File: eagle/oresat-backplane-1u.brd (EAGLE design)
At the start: 82.5 x 213.5 mm, 35 parts

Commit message: oresat-backplane-1u.sch
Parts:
- moved C3 114.5 mm to (32.3, 14.3)
- moved C4 114.5 mm to (42.5, 14.3)
- moved CF2.1 114.5 mm to (13.2, 82.1)
- moved CF2.2 114.5 mm to (41.2, 82.1)
- moved CF2.3 114.5 mm to (19.6, 92.1)
- moved CF3.1 114.5 mm to (13.2, 72.1)
- moved CF3.2 114.5 mm to (41.2, 72.1)
- moved CF4.1 114.5 mm to (13.2, 62.1)
- moved CF4.2 114.5 mm to (41.2, 62.1)
- moved CF5.1 114.5 mm to (13.2, 52.1)
- moved CF5.2 114.5 mm to (41.2, 52.1)
- moved CF6.1 114.5 mm to (13.2, 42.1)
- moved CF6.2 114.5 mm to (41.2, 42.1)
- moved CF7.1 114.5 mm to (13.2, 32.1)
- moved CF7.2 114.5 mm to (41.2, 32.1)
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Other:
- board size 82.5 x 213.5 mm -> 82.5 x 99 mm
- board text added: "OreSat 1U Backplane v1.0 (Frame 1.1)"
- board text removed: "OreSat Backplane v2.1 (Frame 1.1)"

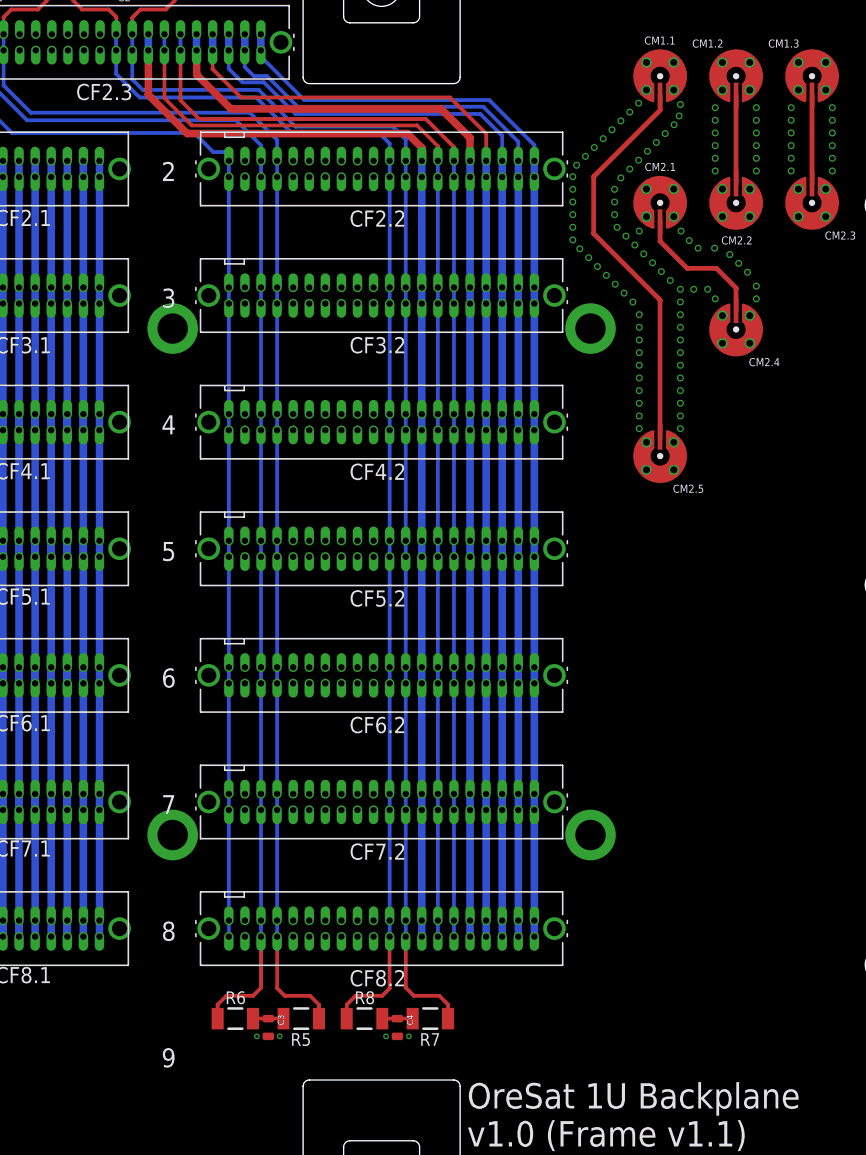
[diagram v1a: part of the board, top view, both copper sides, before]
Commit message: TNAMES cleanup, renamed by card number.
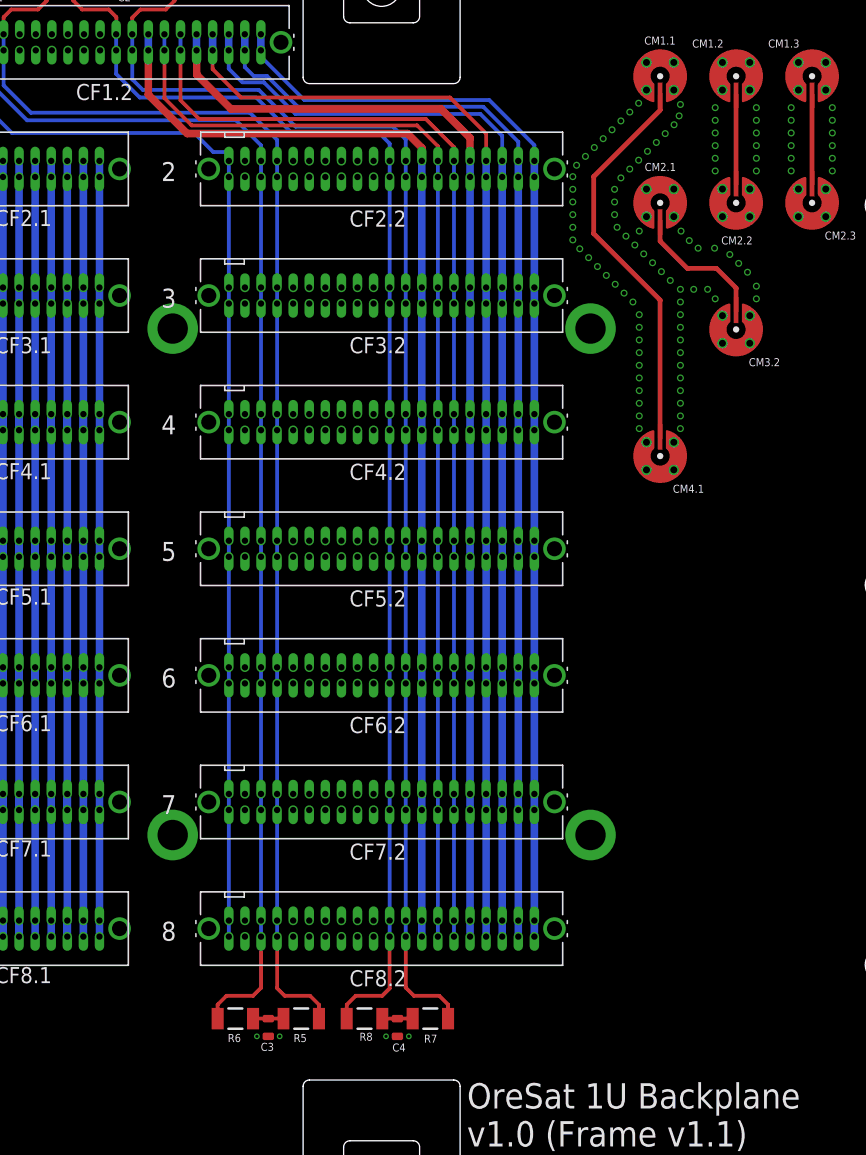
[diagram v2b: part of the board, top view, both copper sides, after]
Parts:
- renumbered CF2.3 to CF1.2, CM2.4 to CM3.2, CM2.5 to CM4.1

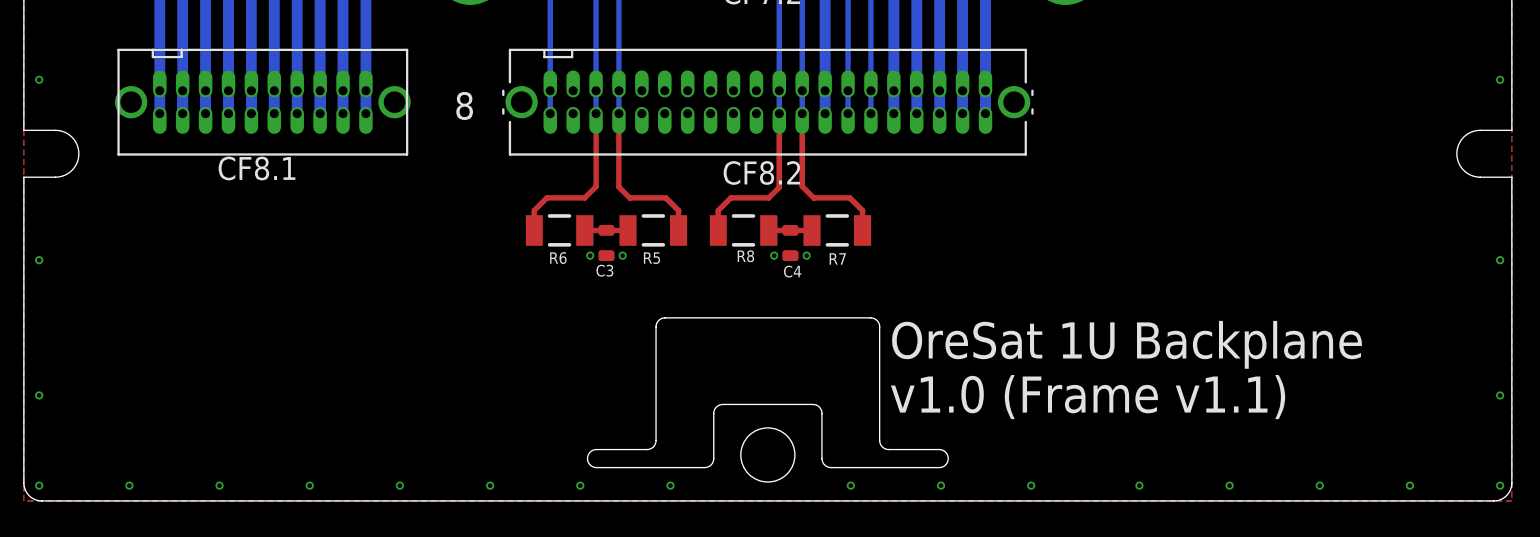
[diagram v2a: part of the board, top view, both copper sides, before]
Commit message: Added 1U -Z end cap connector.
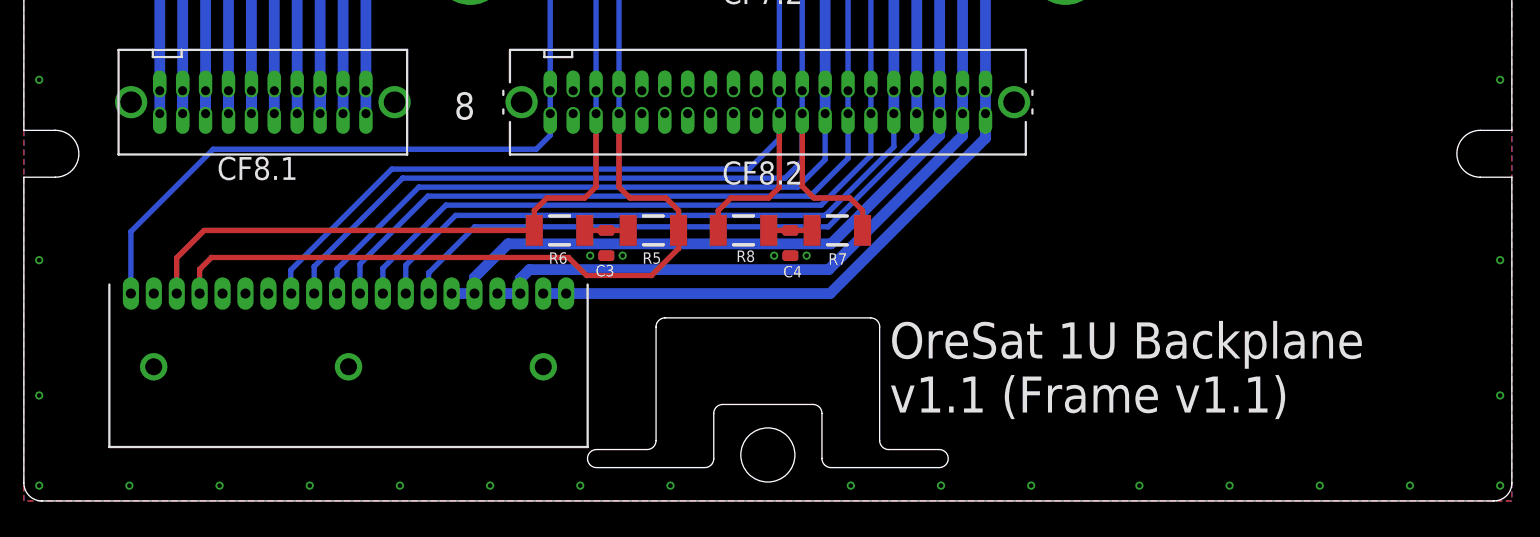
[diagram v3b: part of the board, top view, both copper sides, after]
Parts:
- added J1: 5-104196-5, J-TE-5-104196-5-RA-1.27mm-female-th:5-104196-5
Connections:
- removed net SPARE1: CF1.2.10, CF1.2.9, CF2.2.10, CF2.2.9, CF3.2.10, CF3.2.9, CF4.2.10, CF4.2.9, CF5.2.10, CF5.2.9, CF6.2.10, CF6.2.9, CF7.2.10, CF7.2.9, CF8.2.10, CF8.2.9
- removed net SPARE3: CF1.2.5, CF1.2.6, CF2.2.5, CF2.2.6, CF3.2.5, CF3.2.6, CF4.2.5, CF4.2.6, CF5.2.5, CF5.2.6, CF6.2.5, CF6.2.6, CF7.2.5, CF7.2.6, CF8.2.5, CF8.2.6
- removed net SPARE4: CF1.2.3, CF1.2.4, CF2.2.3, CF2.2.4, CF3.2.3, CF3.2.4, CF4.2.3, CF4.2.4, CF5.2.3, CF5.2.4, CF6.2.3, CF6.2.4, CF7.2.3, CF7.2.4, CF8.2.3, CF8.2.4
- removed net SPARE5: CF1.2.1, CF1.2.2, CF2.2.1, CF2.2.2, CF3.2.1, CF3.2.2, CF4.2.1, CF4.2.2, CF5.2.1, CF5.2.2, CF6.2.1, CF6.2.2, CF7.2.1, CF7.2.2, CF8.2.1, CF8.2.2
- new net SPARE1-TURNSTILE-DPLY: CF1.2.10, CF1.2.9, CF2.2.10, CF2.2.9, CF3.2.10, CF3.2.9, CF4.2.10, CF4.2.9, CF5.2.10, CF5.2.9, CF6.2.10, CF6.2.9, CF7.2.10, CF7.2.9, CF8.2.10, CF8.2.9, J1.13
- new net SPARE3-MAG-PWR: CF1.2.5, CF1.2.6, CF2.2.5, CF2.2.6, CF3.2.5, CF3.2.6, CF4.2.5, CF4.2.6, CF5.2.5, CF5.2.6, CF6.2.5, CF6.2.6, CF7.2.5, CF7.2.6, CF8.2.5, CF8.2.6, J1.15, J1.16
- new net SPARE4-MAG-SCL: CF1.2.3, CF1.2.4, CF2.2.3, CF2.2.4, CF3.2.3, CF3.2.4, CF4.2.3, CF4.2.4, CF5.2.3, CF5.2.4, CF6.2.3, CF6.2.4, CF7.2.3, CF7.2.4, CF8.2.3, CF8.2.4, J1.17, J1.18
- new net SPARE5-MAG-SDA: CF1.2.1, CF1.2.2, CF2.2.1, CF2.2.2, CF3.2.1, CF3.2.2, CF4.2.1, CF4.2.2, CF5.2.1, CF5.2.2, CF6.2.1, CF6.2.2, CF7.2.1, CF7.2.2, CF8.2.1, CF8.2.2, J1.19, J1.20
- net !SD: now also J1.1
- net CAN1_H: now also J1.4
- net CAN1_L: now also J1.3
- net CAN2_H: now also J1.9
- net CAN2_L: now also J1.8
- net GND: now also J1.2, J1.5, J1.6, J1.HD1, J1.HD2, J1.HD3
- net OPD_PWR: now also J1.10
- net OPD_SCL: now also J1.11
- net OPD_SDA: now also J1.12
- net SPARE2: now also J1.14
- net VBUS: now also J1.7
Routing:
- net SPARE1-TURNSTILE-DPLY: track 0.00 -> 123.1 mm
- net SPARE3-MAG-PWR: track 0.00 -> 122.2 mm
- net SPARE4-MAG-SCL: track 0.00 -> 120.5 mm
- net SPARE5-MAG-SDA: track 0.00 -> 118.2 mm
- net SPARE1: track 89.9 -> 0.00 mm
- net SPARE3: track 89.8 -> 0.00 mm
- net SPARE4: track 89.4 -> 0.00 mm
- net SPARE5: track 88.8 -> 0.00 mm
- net OPD_SCL: track 90.6 -> 124.2 mm
- net CAN2_H: track 105.4 -> 139.0 mm
- net OPD_PWR: track 90.4 -> 123.9 mm
- net OPD_SDA: track 90.7 -> 124.1 mm
- net CAN2_L: track 105.2 -> 138.0 mm
- net SPARE2: track 89.9 -> 122.5 mm
- net VBUS: track 0.00 -> 31.8 mm
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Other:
- board text added: "OreSat 1U Backplane v1.1 (Frame v1.1)"
- board text removed: "OreSat 1U Backplane v1.0 (Frame v1.1)"

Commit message: Backplane v1.1!
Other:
- board text added: "OreSat 1U Backplane v1.1 (Frame 1.1)"
- board text removed: "OreSat 1U Backplane v1.0 (Frame 1.1)"
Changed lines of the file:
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@@
 v1.1 (Frame v1.1)</text>
 <text x="34.35" y="4.85" size="2" layer="22" font="vector" rot="MR0">OreSat 1U Backplane
-v1.0 (Frame 1.1)</text>
+v1.1 (Frame 1.1)</text>
 <wire x1="75.75" y1="95.25" x2="6.75" y2="95.25" width="0.001" layer="52"/>
 <wire x1="6.75" y1="95.25" x2="4.25" y2="92.75" width="0.001" layer="52" curve="90"/>

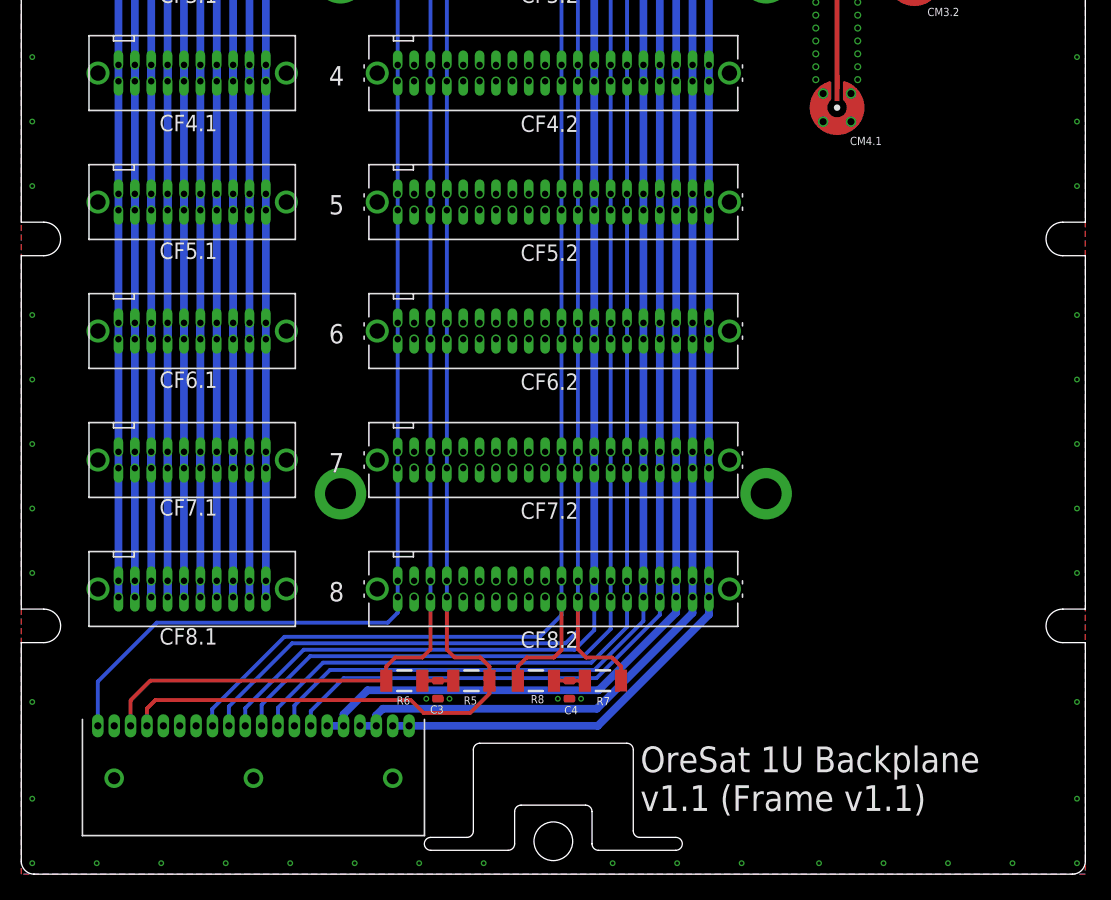
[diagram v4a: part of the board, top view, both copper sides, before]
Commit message: Updated 1U backplane to v1.2. Better position of end cap connector, added debug connector.
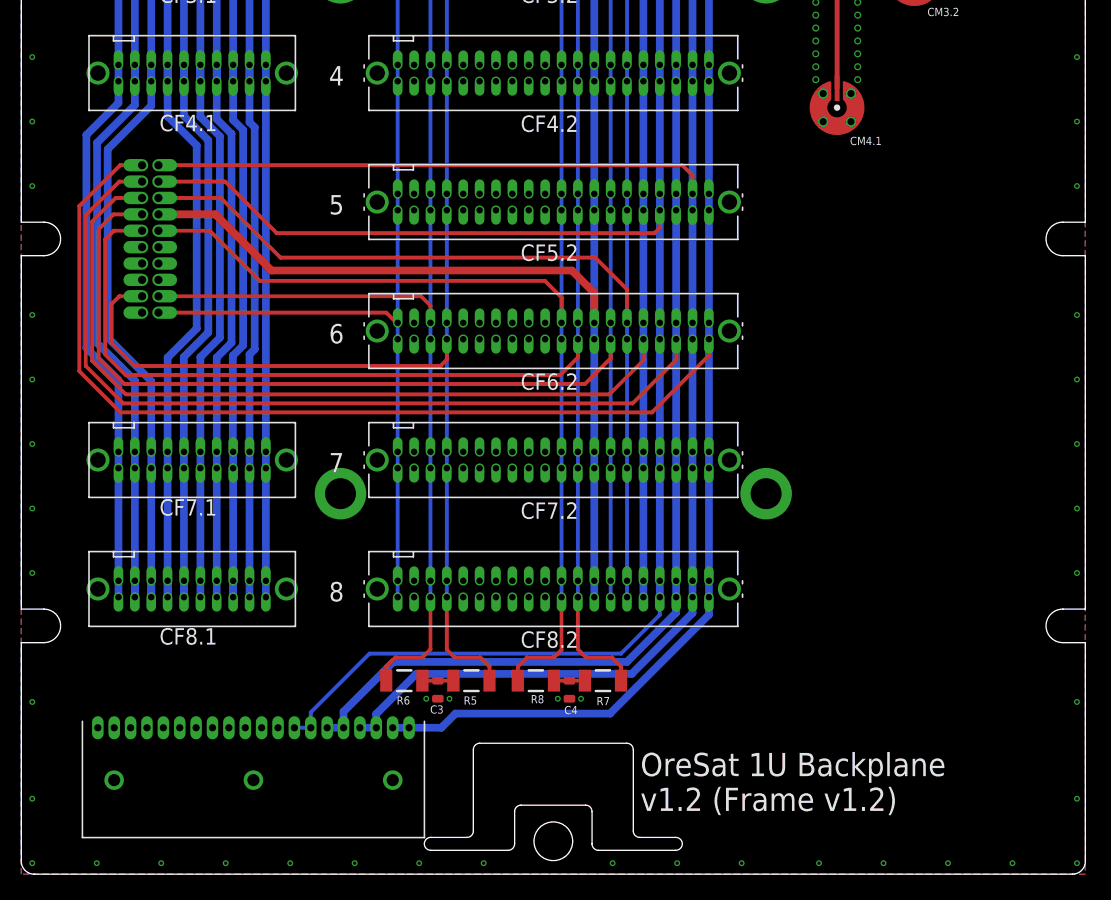
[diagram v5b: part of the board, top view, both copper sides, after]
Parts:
- removed CF5.1, CF6.1: SFM-110-X1-XXX-D-LC, J-Samtec-SFM-110-X1-XXX-D-LC:SFM-110-X1-XXX-D-LC
- added J3: HARWIN-M50-3002045, J-Harwin-M50-3002045-20pin-1.27-F-vertical:HARWIN-M50-30020452
- moved J1 0.15 mm to (18.0, 11.3)
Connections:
- net !SD: now also J3.20; no longer J1.1
- net AUX-1: no longer CF5.1.1, CF5.1.2, CF6.1.1, CF6.1.2
- net AUX-10: no longer CF5.1.19, CF5.1.20, CF6.1.19, CF6.1.20
- net AUX-2: no longer CF5.1.3, CF5.1.4, CF6.1.3, CF6.1.4
- net AUX-3: no longer CF5.1.5, CF5.1.6, CF6.1.5, CF6.1.6
- net AUX-4: no longer CF5.1.7, CF5.1.8, CF6.1.7, CF6.1.8
- net AUX-5: no longer CF5.1.10, CF5.1.9, CF6.1.10, CF6.1.9
- net AUX-6: no longer CF5.1.11, CF5.1.12, CF6.1.11, CF6.1.12
- net AUX-7: no longer CF5.1.13, CF5.1.14, CF6.1.13, CF6.1.14
- net AUX-8: no longer CF5.1.15, CF5.1.16, CF6.1.15, CF6.1.16
- net AUX-9: no longer CF5.1.17, CF5.1.18, CF6.1.17, CF6.1.18
- net CAN1_H: now also J3.17; no longer J1.4
- net CAN1_L: now also J3.18; no longer J1.3
- net CAN2_H: now also J3.9; no longer J1.9
- net CAN2_L: now also J3.10; no longer J1.8
- net GND: now also J1.1, J1.10, J1.11, J1.12, J1.3, J1.4, J1.7, J1.8, J1.9, J3.14, J3.15, J3.16, J3.19; no longer CF5.1.LC1, CF5.1.LC2, CF6.1.LC1, CF6.1.LC2
- net OPD_PWR: now also J3.8; no longer J1.10
- net OPD_SCL: now also J3.7; no longer J1.11
- net OPD_SDA: now also J3.6; no longer J1.12
- net SPARE1-TURNSTILE-DPLY: now also J3.5; no longer J1.13
- net SPARE2: now also J1.13, J3.4
- net SPARE3-MAG-PWR: now also J3.3
- net SPARE4-MAG-SCL: now also J3.2
- net SPARE5-MAG-SDA: now also J3.1
- net VBUS: now also J3.11, J3.12, J3.13; no longer J1.7
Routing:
- net SPARE5-MAG-SDA: track 118.2 -> 190.5 mm
- net SPARE3-MAG-PWR: track 122.2 -> 189.6 mm
- net SPARE2: track 122.5 -> 166.0 mm
- net SPARE4-MAG-SCL: track 120.5 -> 163.9 mm
- net SPARE1-TURNSTILE-DPLY: track 123.1 -> 152.0 mm
- net OPD_SCL: track 124.2 -> 147.3 mm
- net CAN2_H: track 139.0 -> 156.8 mm
- net !SD: track 119.5 -> 108.3 mm
- net OPD_SDA: track 124.1 -> 132.6 mm
- net OPD_PWR: track 123.9 -> 129.0 mm
- net AUX-3: track 67.6 -> 64.5 mm
- net CAN1_H: track 136.9 -> 139.9 mm
- net CAN2_L: track 138.0 -> 140.5 mm
- net AUX-5: track 66.3 -> 63.8 mm
- net AUX-6: track 67.6 -> 65.4 mm
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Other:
- board text added: "-Z End Cap"
- board text added: "DEBUG"
- board text added: "OreSat 1U Backplane v1.2 (Frame 1.2)"
- board text added: "OreSat 1U Backplane v1.2 (Frame v1.2)"
- board text removed: "9"
- board text removed: "OreSat 1U Backplane v1.1 (Frame 1.1)"
- board text removed: "OreSat 1U Backplane v1.1 (Frame v1.1)"
